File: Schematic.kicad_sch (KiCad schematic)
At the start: 31 parts, among them J1 Screw_Terminal_01x04, Q2 HY1707, Q3 S8050, Q4 HY1707, U1 UC2843AQD8R

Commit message: testing lib issue
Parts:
- D4: renamed from D2; Notes (none) -> Markings are not readable on the part
- F1: value Fuse -> ?
- renumbered D1 to D3, Q4 to Q1, TR2 to TR1, RV1 to VR1
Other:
- title: TEST TEXT -> Schematic

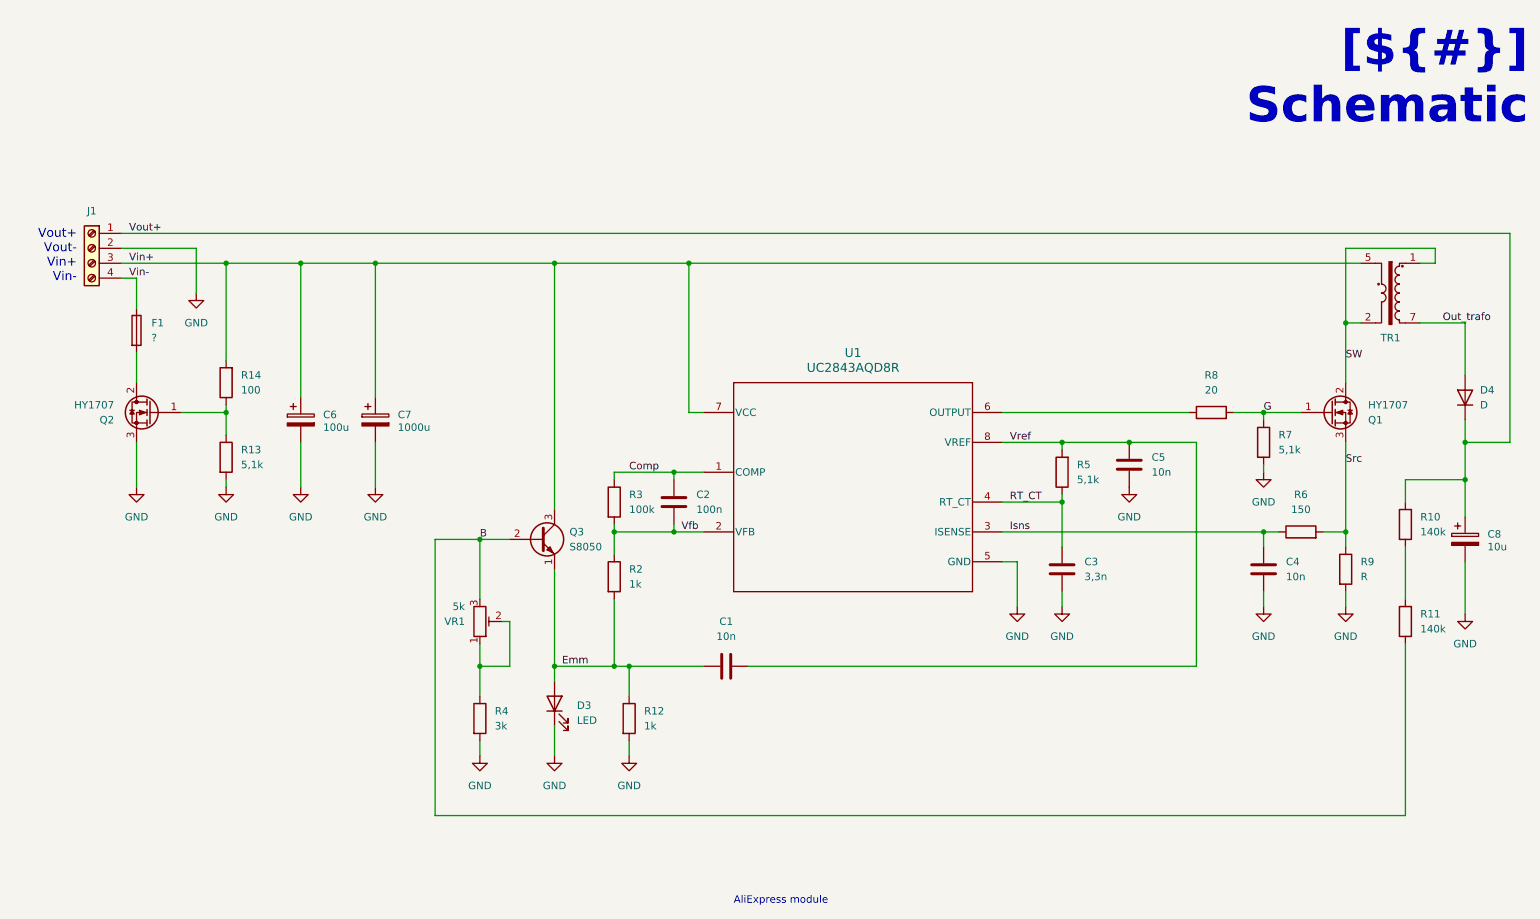
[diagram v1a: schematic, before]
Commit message: Updated some footpints
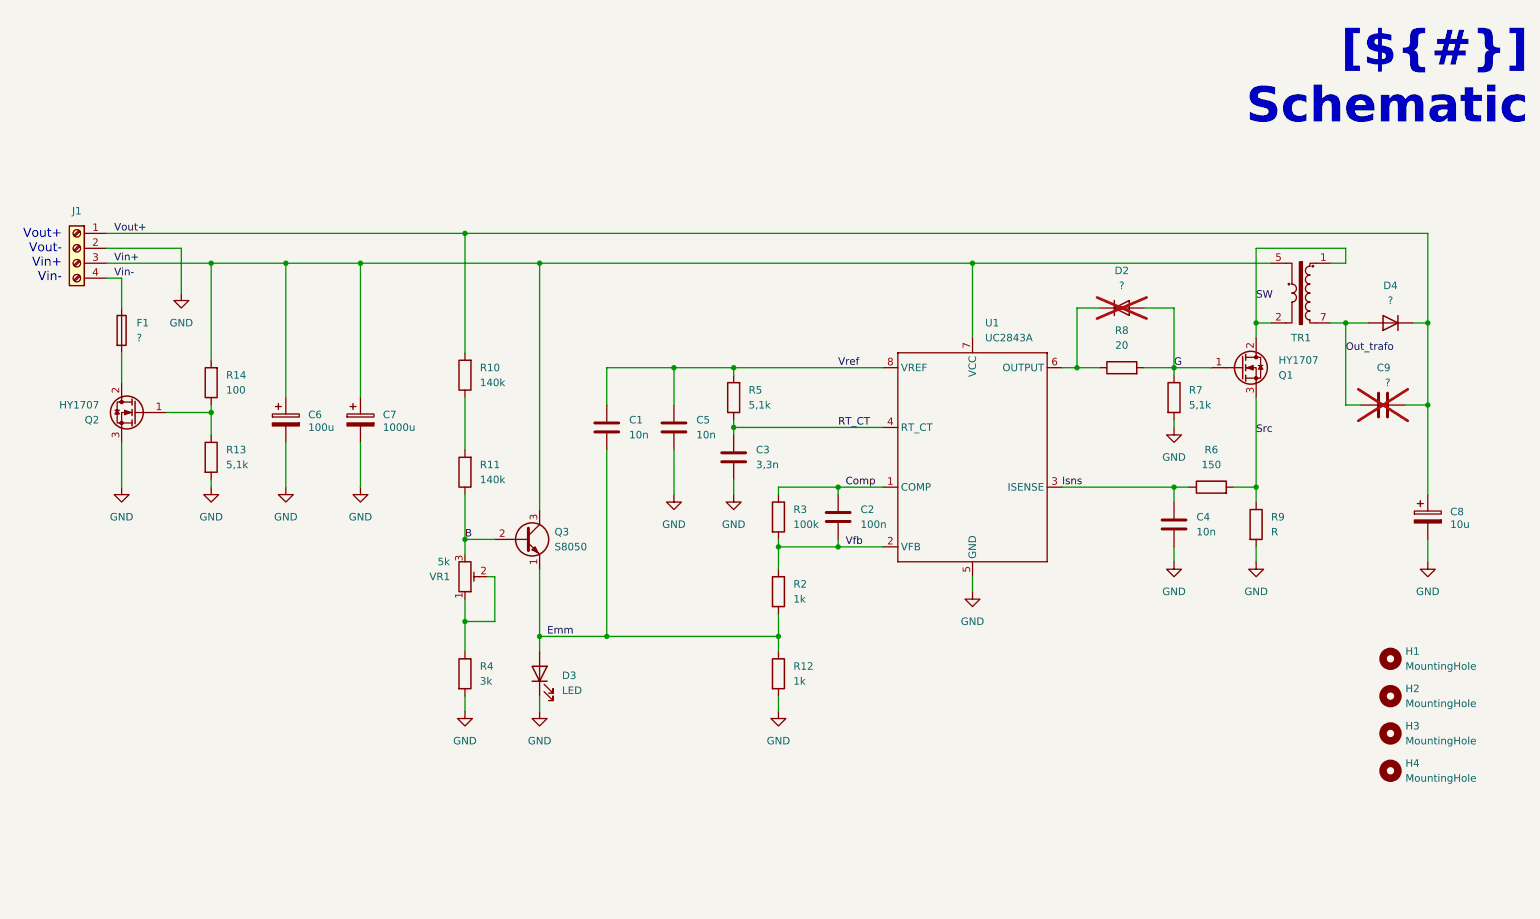
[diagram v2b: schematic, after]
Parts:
- removed U1: UC2843AQD8R, Package_DIP:DIP-8_W7.62mm, symbol 2025-12-06_19-11-20:UC2843AQD8R
- added C9: ?, Capacitor_THT:C_Rect_L7.0mm_W2.0mm_P5.00mm, symbol Device:C
- added D2: ?, Diode_THT:D_A-405_P7.62mm_Horizontal, symbol Device:D
- added H1, H2, H3, H4: MountingHole, MountingHole:MountingHole_2.1mm, symbol Mechanical:MountingHole
- added U1: UC2843A, Package_DIP:DIP-8_W7.62mm, symbol personal:UC2843AQD8R
- C6: footprint Capacitor_THT:CP_Radial_D8.0mm_P3.50mm -> Capacitor_THT:C_Radial_D8.0mm_H11.5mm_P3.50mm
- C7: footprint Capacitor_THT:CP_Radial_D10.0mm_P5.00mm -> Capacitor_THT:C_Radial_D10.0mm_H20.0mm_P5.00mm
- C8: footprint Capacitor_THT:CP_Radial_D10.0mm_P5.00mm -> Capacitor_THT:C_Radial_D10.0mm_H16.0mm_P5.00mm
- D4: value D -> ?
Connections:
- net Comp: now also U1.1 (COMP)
- net G: now also D2.2 (A)
- net GND: now also U1.5 (GND)
- net Isns: now also U1.3 (ISENSE)
- net Out_trafo: now also C9.1
- net RT_CT: now also U1.4 (RT_CT)
- net Vfb: now also U1.2 (VFB)
- net Vin+: now also U1.7 (VCC)
- net Vout+: now also C9.2
- net Vref: now also U1.8 (VREF)
- net at R8.1: now also D2.1 (K), U1.6 (OUTPUT)
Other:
- note removed: "AliExpress module"
- moved on the sheet: C1, C2, C3, C4, C5, C6, C7, C8, D3, D4, F1, J1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

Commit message: Updated terminal block
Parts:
- J1: footprint TerminalBlock:TerminalBlock_MaiXu_MX126-5.0-04P_1x04_P5.00mm -> TerminalBlock_Phoenix:TerminalBlock_Phoenix_MKDS-1,5-4_1x04_P5.00mm_Horizontal
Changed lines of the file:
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@@
 			)
 		)
-		(property "Footprint" "TerminalBlock:TerminalBlock_MaiXu_MX126-5.0-04P_1x04_P5.00mm"
+		(property "Footprint" "TerminalBlock_Phoenix:TerminalBlock_Phoenix_MKDS-1,5-4_1x04_P5.00mm_Horizontal"
 			(at 30.48 50.8 0)
 			(effects
